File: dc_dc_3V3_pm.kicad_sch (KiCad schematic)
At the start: 7 parts

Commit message: added few annotations
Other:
- note added: "Operational current max 1mA TODO: look for more efficient solution"
- note removed: "TODO: check that EN tolerates 24V!"
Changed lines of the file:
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@@
     (stroke (width 0) (type default) (color 0 0 0 0))
   )
-  (text "TODO: check that\nEN tolerates 24V!" (at 104.14 102.235 0)
+  (text "Operational current max 1mA\nTODO: look for more efficient solution"
+    (at 109.22 74.93 0)
     (effects (font (size 1.27 1.27)) (justify left bottom))
   )

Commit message: replaced main MCU, reannotated
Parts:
- gave numbers to parts that had none: 7
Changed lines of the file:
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@@
   (symbol (lib_id "Device:R_Small") (at 137.16 100.33 0) (unit 1)
     (in_bom yes) (on_board yes) (fields_autoplaced)
-    (property "Reference" "R?" (id 0) (at 139.7 99.0599 0)
+    (property "Reference" "R51" (id 0) (at 139.7 99.0599 0)
       (effects (font (size 1.27 1.27)) (justify left))
     )
@@
   (symbol (lib_id "power:GND") (at 123.19 100.33 0) (unit 1)
     (in_bom yes) (on_board yes) (fields_autoplaced)
-    (property "Reference" "#PWR?" (id 0) (at 123.19 106.68 0)
+    (property "Reference" "#PWR0100" (id 0) (at 123.19 106.68 0)
       (effects (font (size 1.27 1.27)) hide)
     )
@@
   (symbol (lib_id "Device:C_Small") (at 132.08 83.82 0) (unit 1)
     (in_bom yes) (on_board yes) (fields_autoplaced)
-    (property "Reference" "C?" (id 0) (at 134.62 82.5562 0)
+    (property "Reference" "C66" (id 0) (at 134.62 82.5562 0)
       (effects (font (size 1.27 1.27)) (justify left))
     )
@@
   (symbol (lib_id "power:GND") (at 166.37 95.25 0) (unit 1)
     (in_bom yes) (on_board yes) (fields_autoplaced)
-    (property "Reference" "#PWR?" (id 0) (at 166.37 101.6 0)
+    (property "Reference" "#PWR099" (id 0) (at 166.37 101.6 0)
       (effects (font (size 1.27 1.27)) hide)
     )
@@
   (symbol (lib_id "Device:C_Small") (at 166.37 92.71 0) (unit 1)
     (in_bom yes) (on_board yes) (fields_autoplaced)
-    (property "Reference" "C?" (id 0) (at 168.91 91.4462 0)
+    (property "Reference" "C68" (id 0) (at 168.91 91.4462 0)
       (effects (font (size 1.27 1.27)) (justify left))
     )
@@
   (symbol (lib_id "Device:L_Small") (at 139.7 90.17 90) (unit 1)
     (in_bom yes) (on_board yes) (fields_autoplaced)
-    (property "Reference" "L?" (id 0) (at 139.7 85.09 90))
+    (property "Reference" "L4" (id 0) (at 139.7 85.09 90))
     (property "Value" "?F" (id 1) (at 139.7 87.63 90))
     (property "Footprint" "" (id 2) (at 139.7 90.17 0)
@@
   (symbol (lib_id "Device:R_Small") (at 144.78 92.71 0) (unit 1)
     (in_bom yes) (on_board yes)
-    (property "Reference" "R?" (id 0) (at 147.32 91.4399 0)
+    (property "Reference" "R50" (id 0) (at 147.32 91.4399 0)
       (effects (font (size 1.27 1.27)) (justify left))
     )
@@
   (symbol (lib_id "power:GND") (at 137.16 102.87 0) (unit 1)
     (in_bom yes) (on_board yes) (fields_autoplaced)
-    (property "Reference" "#PWR?" (id 0) (at 137.16 109.22 0)
+    (property "Reference" "#PWR0101" (id 0) (at 137.16 109.22 0)
       (effects (font (size 1.27 1.27)) hide)
     )
@@
   (symbol (lib_id "New_Library:TPMP2359DJ") (at 121.92 95.25 0) (unit 1)
     (in_bom yes) (on_board yes)
-    (property "Reference" "U?" (id 0) (at 119.38 82.55 0)
+    (property "Reference" "U14" (id 0) (at 119.38 82.55 0)
       (effects (font (size 1.27 1.27)) (justify left))
     )
@@
   (symbol (lib_id "Device:C_Small") (at 156.21 92.71 180) (unit 1)
     (in_bom yes) (on_board yes) (fields_autoplaced)
-    (property "Reference" "C?" (id 0) (at 158.75 91.4335 0)
+    (property "Reference" "C67" (id 0) (at 158.75 91.4335 0)
       (effects (font (size 1.27 1.27)) (justify right))
     )

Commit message: resolved all erc errors
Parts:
- R51: footprint (none) -> Resistor_SMD:R_0603_1608Metric
- renumbered C66 to C65, C67 to C66, C68 to C67, U14 to U15
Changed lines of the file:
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@@
 (kicad_sch (version 20211123) (generator eeschema)
   (paper "A4")
+  (junction (at 184.15 90.17) (diameter 0) (color 0 0 0 0)
+  )
   (junction (at 109.22 90.17) (diameter 0) (color 0 0 0 0)
   )
@@
     (stroke (width 0) (type default) (color 0 0 0 0))
   )
+  (wire (pts (xy 184.15 90.17) (xy 185.42 90.17))
+    (stroke (width 0) (type default) (color 0 0 0 0))
+  )
   (wire (pts (xy 132.08 81.28) (xy 123.19 81.28))
     (stroke (width 0) (type default) (color 0 0 0 0))
@@
     (stroke (width 0) (type default) (color 0 0 0 0))
   )
-  (wire (pts (xy 166.37 90.17) (xy 181.61 90.17))
+  (wire (pts (xy 166.37 90.17) (xy 184.15 90.17))
     (stroke (width 0) (type default) (color 0 0 0 0))
   )
@@
     (effects (font (size 1.27 1.27)) (justify left bottom))
   )
-  (hierarchical_label "+3.3V" (shape input) (at 181.61 90.17 0)
+  (hierarchical_label "+3.3V" (shape input) (at 185.42 90.17 0)
     (effects (font (size 1.27 1.27)) (justify left))
   )
@@
       (effects (font (size 1.27 1.27)) (justify left))
     )
-    (property "Footprint" "" (id 2) (at 137.16 100.33 0)
+    (property "Footprint" "Resistor_SMD:R_0603_1608Metric" (id 2) (at 137.16 100.33 0)
       (effects (font (size 1.27 1.27)) hide)
     )
@@
   (symbol (lib_id "power:GND") (at 123.19 100.33 0) (unit 1)
     (in_bom yes) (on_board yes) (fields_autoplaced)
-    (property "Reference" "#PWR0100" (id 0) (at 123.19 106.68 0)
+    (property "Reference" "#PWR094" (id 0) (at 123.19 106.68 0)
       (effects (font (size 1.27 1.27)) hide)
     )
@@
   (symbol (lib_id "Device:C_Small") (at 132.08 83.82 0) (unit 1)
     (in_bom yes) (on_board yes) (fields_autoplaced)
-    (property "Reference" "C66" (id 0) (at 134.62 82.5562 0)
+    (property "Reference" "C65" (id 0) (at 134.62 82.5562 0)
       (effects (font (size 1.27 1.27)) (justify left))
     )
@@
   (symbol (lib_id "power:GND") (at 166.37 95.25 0) (unit 1)
     (in_bom yes) (on_board yes) (fields_autoplaced)
-    (property "Reference" "#PWR099" (id 0) (at 166.37 101.6 0)
+    (property "Reference" "#PWR093" (id 0) (at 166.37 101.6 0)
       (effects (font (size 1.27 1.27)) hide)
     )
@@
   (symbol (lib_id "Device:C_Small") (at 166.37 92.71 0) (unit 1)
     (in_bom yes) (on_board yes) (fields_autoplaced)
-    (property "Reference" "C68" (id 0) (at 168.91 91.4462 0)
+    (property "Reference" "C67" (id 0) (at 168.91 91.4462 0)
       (effects (font (size 1.27 1.27)) (justify left))
     )
@@
     (pin "2")
   )
+  (symbol (lib_id "power:PWR_FLAG") (at 184.15 90.17 0) (unit 1)
+    (in_bom yes) (on_board yes) (fields_autoplaced)
+    (property "Reference" "#FLG013" (id 0) (at 184.15 88.265 0)
+      (effects (font (size 1.27 1.27)) hide)
+    )
+    (property "Value" "PWR_FLAG" (id 1) (at 184.15 85.09 0))
+    (property "Footprint" "" (id 2) (at 184.15 90.17 0)
+      (effects (font (size 1.27 1.27)) hide)
+    )
+    (property "Datasheet" "~" (id 3) (at 184.15 90.17 0)
+      (effects (font (size 1.27 1.27)) hide)
+    )
+    (pin "1")
+  )
   (symbol (lib_id "Device:R_Small") (at 144.78 92.71 0) (unit 1)
     (in_bom yes) (on_board yes)
@@
   (symbol (lib_id "power:GND") (at 137.16 102.87 0) (unit 1)
     (in_bom yes) (on_board yes) (fields_autoplaced)
-    (property "Reference" "#PWR0101" (id 0) (at 137.16 109.22 0)
+    (property "Reference" "#PWR095" (id 0) (at 137.16 109.22 0)
       (effects (font (size 1.27 1.27)) hide)
     )
@@
   (symbol (lib_id "New_Library:TPMP2359DJ") (at 121.92 95.25 0) (unit 1)
     (in_bom yes) (on_board yes)
-    (property "Reference" "U14" (id 0) (at 119.38 82.55 0)
+    (property "Reference" "U15" (id 0) (at 119.38 82.55 0)
       (effects (font (size 1.27 1.27)) (justify left))
     )
@@
   (symbol (lib_id "Device:C_Small") (at 156.21 92.71 180) (unit 1)
     (in_bom yes) (on_board yes) (fields_autoplaced)
-    (property "Reference" "C67" (id 0) (at 158.75 91.4335 0)
+    (property "Reference" "C66" (id 0) (at 158.75 91.4335 0)
       (effects (font (size 1.27 1.27)) (justify right))
     )

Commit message: updated footprints from schematics
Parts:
- R51: LCSC (none) -> C25804
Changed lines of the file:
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@@
       (effects (font (size 1.27 1.27)) hide)
     )
-    (property "Datasheet" "~" (id 3) (at 137.16 100.33 0)
+    (property "Datasheet" "https://datasheet.lcsc.com/lcsc/2206010045_UNI-ROYAL-Uniroyal-Elec-0603WAF1002T5E_C25804.pdf" (id 3) (at 137.16 100.33 0)
       (effects (font (size 1.27 1.27)) hide)
     )
+    (property "LCSC" "C25804" (id 4) (at 137.16 100.33 0)
+      (effects (font (size 1.27 1.27)) hide)
+    )

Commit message: updated mounting hole locations and corrected designators for all converters
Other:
- note added: "Operational current max 200mA TODO: look for more efficient solution"
- note removed: "Operational current max 1mA TODO: look for more efficient solution"
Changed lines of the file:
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@@
     (stroke (width 0) (type default) (color 0 0 0 0))
   )
-  (text "Operational current max 1mA\nTODO: look for more efficient solution"
+  (text "Operational current max 200mA\nTODO: look for more efficient solution"
     (at 109.22 74.93 0)
     (effects (font (size 1.27 1.27)) (justify left bottom))

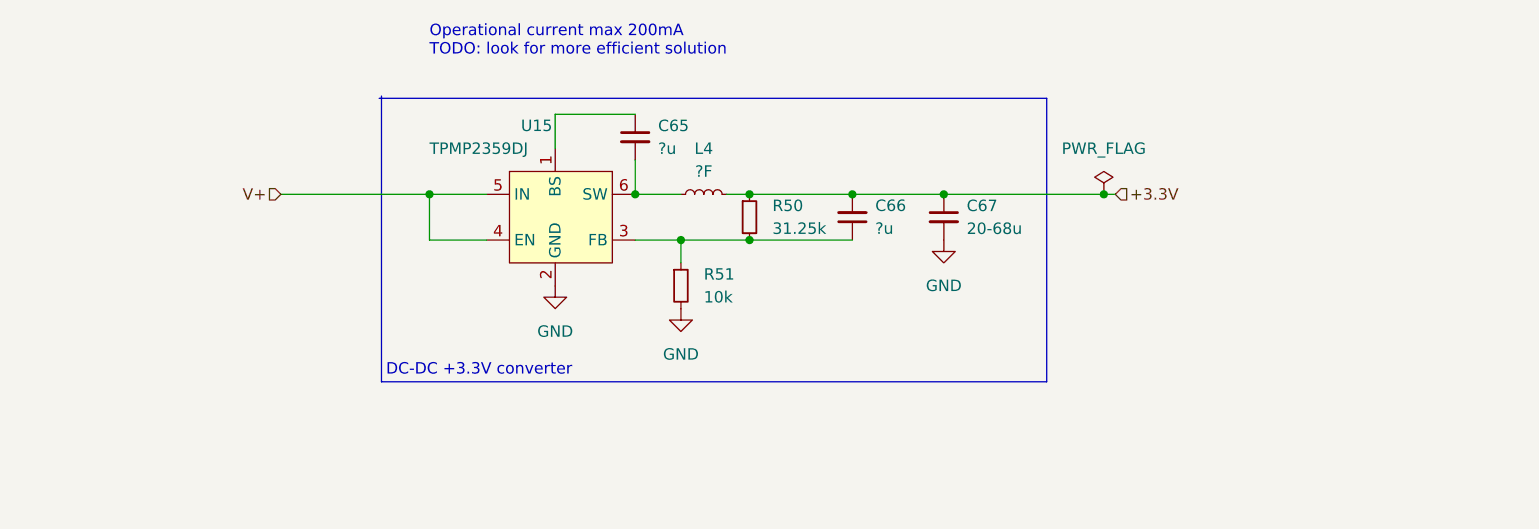
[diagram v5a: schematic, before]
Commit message: optimized component selection, assigned missing LCSC part numbers
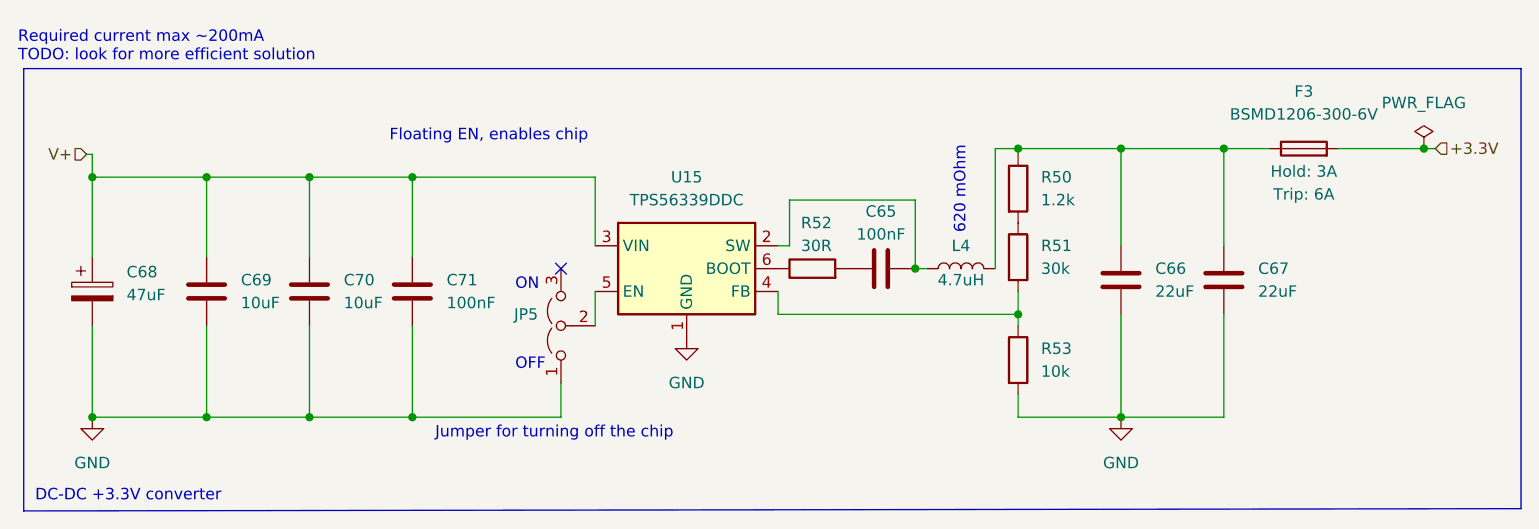
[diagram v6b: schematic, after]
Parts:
- removed C65, C66: ?u, symbol Device:C_Small
- removed C67: 20-68u, symbol Device:C_Small
- removed L4: ?F, symbol Device:L_Small
- removed R50: 31.25k, symbol Device:R_Small
- removed R51: 10k, Resistor_SMD:R_0603_1608Metric, symbol Device:R_Small
- removed U15: TPMP2359DJ, symbol New_Library:TPMP2359DJ
- added C65, C71: 100nF, Capacitor_SMD:C_0805_2012Metric, symbol Device:C
- added C66, C67: 22uF, Capacitor_SMD:C_1206_3216Metric, symbol Device:C
- added C68: 47uF, Capacitor_SMD:C_1206_3216Metric, symbol Device:C_Polarized
- added C69, C70: 10uF, Capacitor_SMD:C_1206_3216Metric, symbol Device:C
- added F3: BSMD1206-300-6V, Fuse:Fuse_1206_3216Metric_Pad1.42x1.75mm_HandSolder, symbol Device:Fuse
- added JP5: (no value), Connector_PinHeader_2.54mm:PinHeader_1x03_P2.54mm_Vertical, symbol Jumper:Jumper_3_Open
- added L4: 4.7uH, Robotont:IND-FXL1040-4R7-M, symbol Device:L
- added R50: 1.2k, Resistor_SMD:R_0603_1608Metric, symbol Device:R
- added R51: 30k, Resistor_SMD:R_0603_1608Metric, symbol Device:R
- added R52: 30R, Resistor_SMD:R_0603_1608Metric, symbol Device:R
- added R53: 10k, Resistor_SMD:R_0603_1608Metric, symbol Device:R
- added U15: TPS56339DDC, Package_TO_SOT_SMD:TSOT-23-6, symbol Regulator_Switching:TPS56339DDC
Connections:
- net +3.3V: now also F3.2
- net GND: now also C66.2, C67.2, C68.2, C69.2, C70.2, C71.2, JP5.1 (A), R53.2, U15.1 (GND)
- net V+: now also C68.1, C69.1, C70.1, C71.1, U15.3 (VIN)
- new net: C66.1, C67.1, F3.1, L4.2, R50.1
- new net: R50.2, R51.1
- new net: R51.2, R53.1, U15.4 (FB)
- new net: R52.1, U15.6 (BOOT)
- new net: C65.1, R52.2
- new net: C65.2, L4.1, U15.2 (SW)
- new net: JP5.2 (C), U15.5 (EN)
- no-connect marks 0 -> 1
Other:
- note added: "620 mOhm"
- note added: "Floating EN, enables chip"
- note added: "Jumper for turning off the chip"
- note added: "OFF"
- note added: "ON"
- note added: "Required current max ~200mA TODO: look for more efficient solution"
- note removed: "Operational current max 200mA TODO: look for more efficient solution"
